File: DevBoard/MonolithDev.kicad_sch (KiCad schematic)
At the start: 4 parts

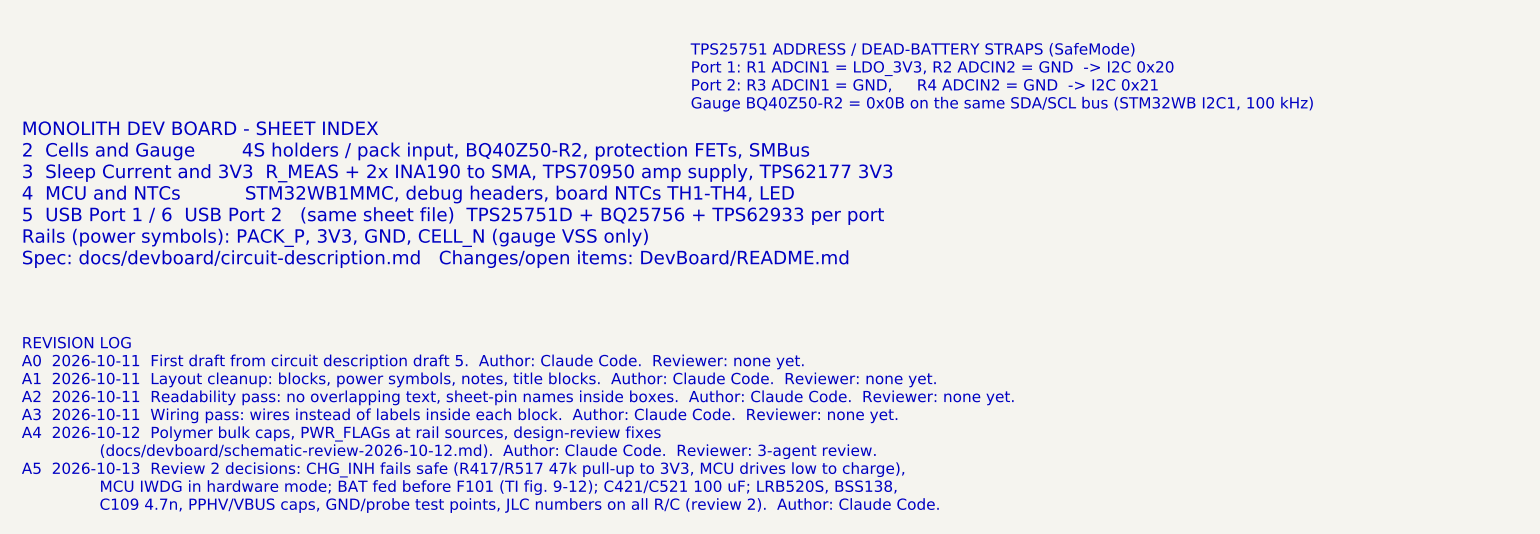
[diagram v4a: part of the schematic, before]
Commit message: Dev board: silkscreen purpose/pinout labels; sleep-current SMAs to test loops
- Silkscreen: WAKE / RESET / AMP EN / MEAS PWR / SWD part labels and pin
  labels on J101, J102-J107, J103, J104, J303, J402/J502, J301 pin 1
  (place_parts.py PIN_LABELS / PART_LABELS; README item 30).
- J201/J202 vertical SMAs removed: OUT_LO/OUT_HI probed on TP201/TP202, each
  with a GND loop (TP208/TP209) 4.5 mm away, in a row on the bottom edge.
  R204/R205 49.9R kept (README item 31; docs updated).
- Renders, 2D exports and schematic PDF regenerated.

Co-Authored-By: Claude Opus 5.5 <noreply@anthropic.com>
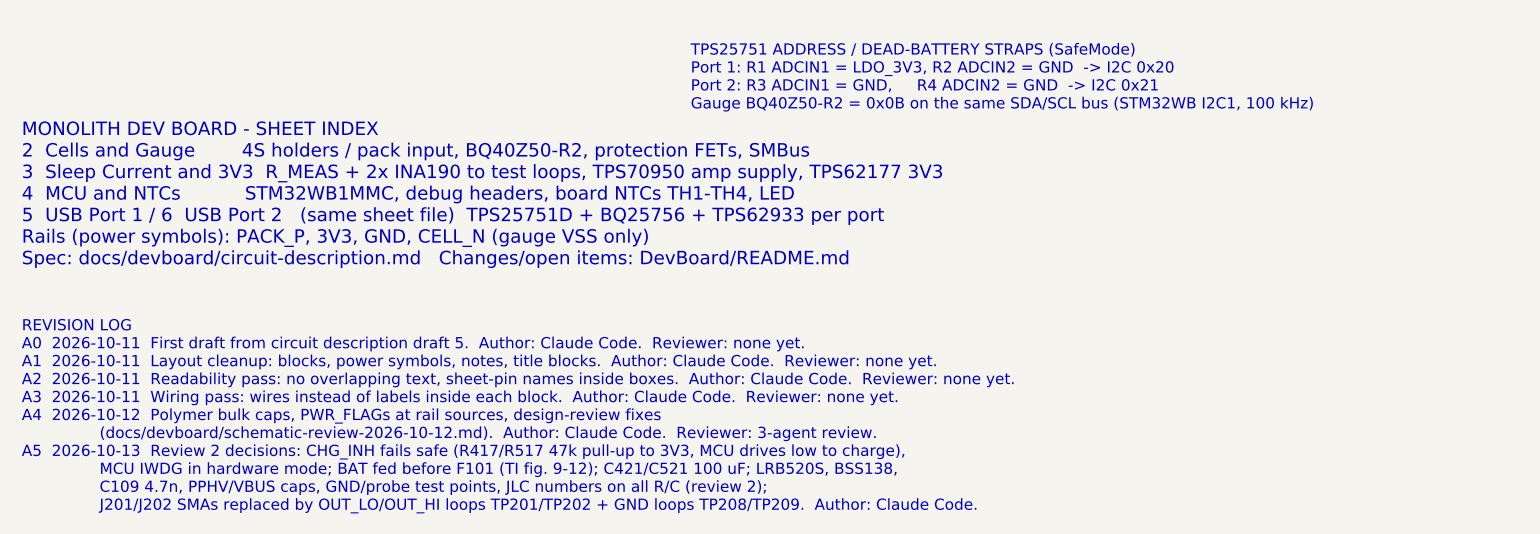
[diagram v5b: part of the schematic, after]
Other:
- note added: "MONOLITH DEV BOARD - SHEET INDEX 2 Cells and Gauge 4S holders / pack input, BQ40Z50-R2, protection FETs, SMBus 3 Sleep Current and 3V3 R_MEAS + 2x INA190 to test loops, TPS70950 amp supply, TPS62177 3V3 4 MCU and NTCs STM32WB1MMC, debug headers, board NTCs TH1-TH4, LED 5 USB Port 1 / 6 USB Port 2 (same sheet file) TPS25751D + BQ25756 + TPS62933 per port Rails (power symbols): PACK_P, 3V3, GND, CE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"
- note removed: "MONOLITH DEV BOARD - SHEET INDEX 2 Cells and Gauge 4S holders / pack input, BQ40Z50-R2, protection FETs, SMBus 3 Sleep Current and 3V3 R_MEAS + 2x INA190 to SMA, TPS70950 amp supply, TPS62177 3V3 4 MCU and NTCs STM32WB1MMC, debug headers, board NTCs TH1-TH4, LED 5 USB Port 1 / 6 USB Port 2 (same sheet file) TPS25751D + BQ25756 + TPS62933 per port Rails (power symbols): PACK_P, 3V3, GND, CELL_N (g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"
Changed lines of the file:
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@@
 		(comment 3 "Not reviewed, laid out, built or tested")
 	)
-	(text "MONOLITH DEV BOARD - SHEET INDEX\n2  Cells and Gauge        4S holders / pack input, BQ40Z50-R2, protection FETs, SMBus\n3  Sleep Current and 3V3  R_MEAS + 2x INA190 to SMA, TPS70950 amp supply, TPS62177 3V3\n4  MCU and NTCs           STM32WB1MMC, debug headers, board NTCs TH1-TH4, LED\n5  USB Port 1 / 6  USB Port 2   (same sheet file)  TPS25751D + BQ25756 + TPS62933 per port\nRails (power symbols): PACK_P, 3V3, GND, CELL_N (gauge VSS only)\nSpec: docs/devboard/circuit-description.md   Changes/open items: DevBoard/README.md"
+	(text "MONOLITH DEV BOARD - SHEET INDEX\n2  Cells and Gauge        4S holders / pack input, BQ40Z50-R2, protection FETs, SMBus\n3  Sleep Current and 3V3  R_MEAS + 2x INA190 to test loops, TPS70950 amp supply, TPS62177 3V3\n4  MCU and NTCs           STM32WB1MMC, debug headers, board NTCs TH1-TH4, LED\n5  USB Port 1 / 6  USB Port 2   (same sheet file)  TPS25751D + BQ25756 + TPS62933 per port\nRails (power symbols): PACK_P, 3V3, GND, CELL_N (gauge VSS only)\nSpec: docs/devboard/circuit-description.md   Changes/open items: DevBoard/README.md"
 		(exclude_from_sim no)
 		(at 30.48 205.74 0)
@@
 		)
 	)
-	(text "REVISION LOG\nA0  2026-10-11  First draft from circuit description draft 5.  Author: Claude Code.  Reviewer: none yet.\nA1  2026-10-11  Layout cleanup: blocks, power symbols, notes, title blocks.  Author: Claude Code.  Reviewer: none yet.\nA2  2026-10-11  Readability pass: no overlapping text, sheet-pin names inside boxes.  Author: Claude Code.  Reviewer: none yet.\nA3  2026-10-11  Wiring pass: wires instead of labels inside each block.  Author: Claude Code.  Reviewer: none yet.\nA4  2026-10-12  Polymer bulk caps, PWR_FLAGs at rail sources, design-review fixes\n                (docs/devboard/schematic-review-2026-10-12.md).  Author: Claude Code.  Reviewer: 3-agent review.\nA5  2026-10-13  Review 2 decisions: CHG_INH fails safe (R417/R517 47k pull-up to 3V3, MCU drives low to charge),\n                MCU IWDG in hardware mode; BAT fed before F101 (TI fig. 9-12); C421/C521 100 uF; LRB520S, BSS138,\n                C109 4.7n, PPHV/VBUS caps, GND/probe test points, JLC numbers on all R/C (review 2).  Author: Claude Code."
+	(text "REVISION LOG\nA0  2026-10-11  First draft from circuit description draft 5.  Author: Claude Code.  Reviewer: none yet.\nA1  2026-10-11  Layout cleanup: blocks, power symbols, notes, title blocks.  Author: Claude Code.  Reviewer: none yet.\nA2  2026-10-11  Readability pass: no overlapping text, sheet-pin names inside boxes.  Author: Claude Code.  Reviewer: none yet.\nA3  2026-10-11  Wiring pass: wires instead of labels inside each block.  Author: Claude Code.  Reviewer: none yet.\nA4  2026-10-12  Polymer bulk caps, PWR_FLAGs at rail sources, design-review fixes\n                (docs/devboard/schematic-review-2026-10-12.md).  Author: Claude Code.  Reviewer: 3-agent review.\nA5  2026-10-13  Review 2 decisions: CHG_INH fails safe (R417/R517 47k pull-up to 3V3, MCU drives low to charge),\n                MCU IWDG in hardware mode; BAT fed before F101 (TI fig. 9-12); C421/C521 100 uF; LRB520S, BSS138,\n                C109 4.7n, PPHV/VBUS caps, GND/probe test points, JLC numbers on all R/C (review 2);\n                J201/J202 SMAs replaced by OUT_LO/OUT_HI loops TP201/TP202 + GND loops TP208/TP209.  Author: Claude Code."
 		(exclude_from_sim no)
 		(at 30.48 233.68 0)

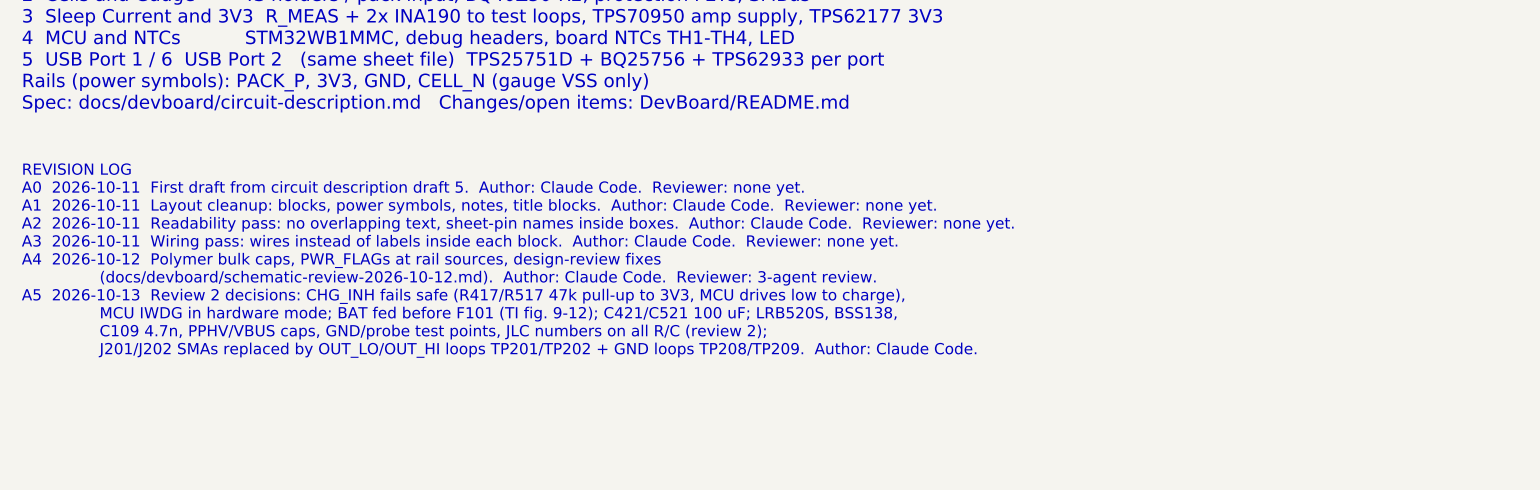
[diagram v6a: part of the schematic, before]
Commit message: Dev board: USB-C liquid detection, schematic review 3 fixes, new datasheets
Liquid detection (TPS25751 datasheet 9.2.2.2, both ports): TPD2S300 U405/U505
on SBU1/SBU2 into GPIO4/5, switched 100k pull-up / 1M pull-down (Q403-Q406)
on GPIO6/7. R440/R540 short D+/D- (passive BC1.2 DCP); D403/D503 removed.

Schematic review 3 (docs/devboard/schematic-review-3-2026-10-14.md):
- H1: TPD2S300 FLT -> GPIO3 fault input (SBU_FLT, R441 pull-up), as on
  TI's TPS25751EVM, so a VBUS-SBU short turns VBUS off.
- H2: R442/R443 hold the liquid-detect FETs off while GPIO6/7 are Hi-Z.
- H3: BQ25756 tuning parts from the EVM: 0R in gate and BTST lines
  (R444-R449), DNP RC snubbers on SW1/SW2 (R450/C454, R451/C455).
- H4: MonolithDev:TPS25751D, stock symbol with GPIO11 bidirectional;
  ERC now 0 errors, 8 expected GPIO-to-GND warnings.
- Gauge data flash and handling rules (Min Blow Fuse Voltage 10.5 V,
  COV Delay 1 s, no cell hot-swap with power on) in the bring-up
  checklist and gauge sheet note 15.
- Docs: A6 revision log, power budget, circuit description, README
  items 16/34/35/36.

Datasheets and app notes added (sources.csv): BQ2947, WSFB1514, TPD2S300,
BQ40Z50-R2 TRM, SLUA660, BQ25756 and TPS25751 EVM guides, discretes.

Co-Authored-By: Claude Opus 5.5 <noreply@anthropic.com>
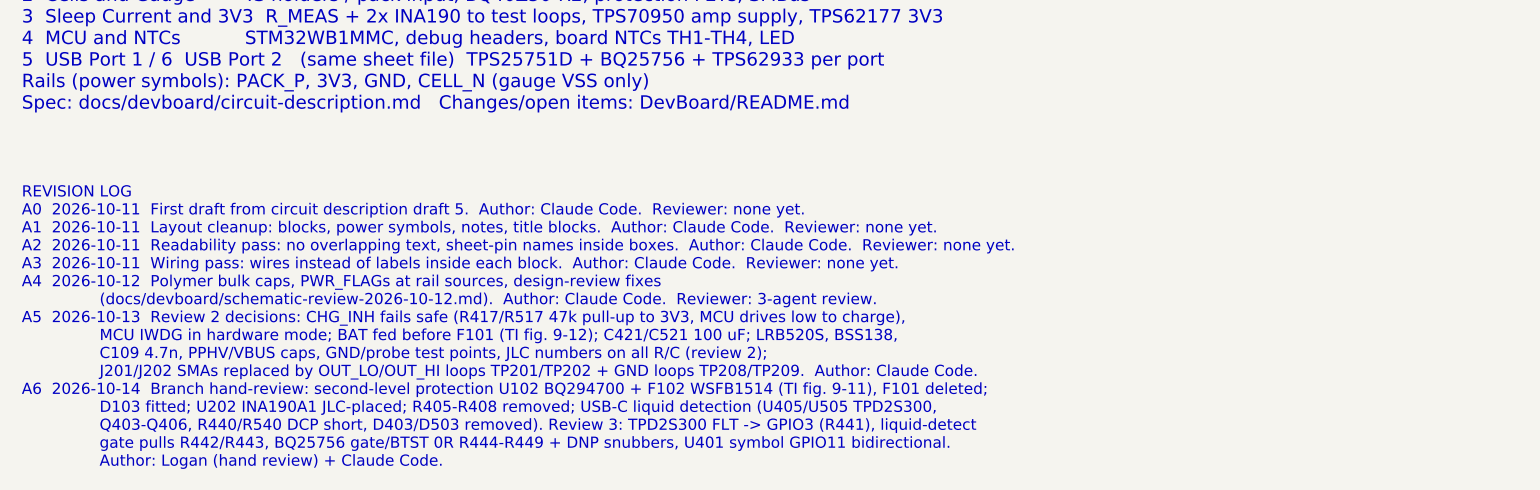
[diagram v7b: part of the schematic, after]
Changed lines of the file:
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@@
 		)
 	)
-	(text "REVISION LOG\nA0  2026-10-11  First draft from circuit description draft 5.  Author: Claude Code.  Reviewer: none yet.\nA1  2026-10-11  Layout cleanup: blocks, power symbols, notes, title blocks.  Author: Claude Code.  Reviewer: none yet.\nA2  2026-10-11  Readability pass: no overlapping text, sheet-pin names inside boxes.  Author: Claude Code.  Reviewer: none yet.\nA3  2026-10-11  Wiring pass: wires instead of labels inside each block.  Author: Claude Code.  Reviewer: none yet.\nA4  2026-10-12  Polymer bulk caps, PWR_FLAGs at rail sources, design-review fixes\n                (docs/devboard/schematic-review-2026-10-12.md).  Author: Claude Code.  Reviewer: 3-agent review.\nA5  2026-10-13  Review 2 decisions: CHG_INH fails safe (R417/R517 47k pull-up to 3V3, MCU drives low to charge),\n                MCU IWDG in hardware mode; BAT fed before F101 (TI fig. 9-12); C421/C521 100 uF; LRB520S, BSS138,\n                C109 4.7n, PPHV/VBUS caps, GND/probe test points, JLC numbers on all R/C (review 2);\n                J201/J202 SMAs replaced by OUT_LO/OUT_HI loops TP201/TP202 + GND loops TP208/TP209.  Author: Claude Code."
+	(text "REVISION LOG\nA0  2026-10-11  First draft from circuit description draft 5.  Author: Claude Code.  Reviewer: none yet.\nA1  2026-10-11  Layout cleanup: blocks, power symbols, notes, title blocks.  Author: Claude Code.  Reviewer: none yet.\nA2  2026-10-11  Readability pass: no overlapping text, sheet-pin names inside boxes.  Author: Claude Code.  Reviewer: none yet.\nA3  2026-10-11  Wiring pass: wires instead of labels inside each block.  Author: Claude Code.  Reviewer: none yet.\nA4  2026-10-12  Polymer bulk caps, PWR_FLAGs at rail sources, design-review fixes\n                (docs/devboard/schematic-review-2026-10-12.md).  Author: Claude Code.  Reviewer: 3-agent review.\nA5  2026-10-13  Review 2 decisions: CHG_INH fails safe (R417/R517 47k pull-up to 3V3, MCU drives low to charge),\n                MCU IWDG in hardware mode; BAT fed before F101 (TI fig. 9-12); C421/C521 100 uF; LRB520S, BSS138,\n                C109 4.7n, PPHV/VBUS caps, GND/probe test points, JLC numbers on all R/C (review 2);\n                J201/J202 SMAs replaced by OUT_LO/OUT_HI loops TP201/TP202 + GND loops TP208/TP209.  Author: Claude Code.\nA6  2026-10-14  Branch hand-review: second-level protection U102 BQ294700 + F102 WSFB1514 (TI fig. 9-11), F101 deleted;\n                D103 fitted; U202 INA190A1 JLC-placed; R405-R408 removed; USB-C liquid detection (U405/U505 TPD2S300,\n                Q403-Q406, R440/R540 DCP short, D403/D503 removed). Review 3: TPD2S300 FLT -> GPIO3 (R441), liquid-detect\n                gate pulls R442/R443, BQ25756 gate/BTST 0R R444-R449 + DNP snubbers, U401 symbol GPIO11 bidirectional.\n                Author: Logan (hand review) + Claude Code."
 		(exclude_from_sim no)
-		(at 30.48 233.68 0)
+		(at 30.48 246.38 0)
 		(effects
 			(font
